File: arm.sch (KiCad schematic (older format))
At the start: 96 parts, among them J1 MICROSD_SOCKET_SPI, M1 MOTOR, P1 MicroUSB, P2 HC-05/06, Q1 MOSFET_N, Q2 IRLML2246TRPBF, Q3 IRLML2246TRPBF, Q5 IRLML2246TRPBF, Q6 IRLML2246TRPBF, Q7 IRLML2246TRPBF, Q8 IRLML2246TRPBF, Q9 IRLML2246TRPBF, U3 LTC2942-1, U4 HMC5883L, U5 MPU6050, U7 BMP085, X1 8 mHz, X2 32.768(MS3V-T1R)

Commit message: Rearranged MOSFET pullup resistors, ~CHARGE and ALERT moved to PC2 and PC3
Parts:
- added R? (x3): 300R, ~, symbol R
- R10, R12, R17, R20, R?: value 1M -> 100k
- R14, R18: value 10k -> 100k
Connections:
- net SD_CD is gone; now on net ~CHARGE: J1.9 (Card_Detect), U?.24 (ADC1_IN14/PC4)
- net ALERT: now also U?.10 (ADC1_IN12/PC2); no longer U?.2 (PC13/TAMPER_RTC)
- net NSS2: now also U?.51 (PC10); no longer U?.52 (PC11)
- net RING_O1: now also R?.2
- net RING_O2: now also R?.2
- net RING_O3: now also R?.2
- net ~CHARGE: now also U?.11 (ADC1_IN13/PC3); no longer U?.51 (PC10)
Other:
- moved on the sheet: D1, M1, Q2, R10, R7
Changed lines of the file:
@@
 P 4750 5200
 F 0 "R12" V 4830 5200 40  0000 C CNN
-F 1 "1M" V 4757 5201 40  0000 C CNN
+F 1 "100k" V 4757 5201 40  0000 C CNN
 F 2 "~" V 4680 5200 30  0000 C CNN
 F 3 "~" H 4750 5200 30  0000 C CNN
@@
 	1    0    0    -1
 $EndComp
-Text GLabel 7900 3600 2    60   Output ~ 0
+Text GLabel 8000 3600 2    60   Output ~ 0
 ~BT_PWR_ENABLE
-Text GLabel 4050 2400 0    60   Input ~ 0
+Text GLabel 7200 3550 2    60   Input ~ 0
 ALERT
 $Comp
@@
 L +3.3V #PWR033
 U 1 1 52E31088
-P 13850 2600
-F 0 "#PWR033" H 13850 2560 30  0001 C CNN
-F 1 "+3.3V" H 13850 2710 30  0000 C CNN
-F 2 "" H 13850 2600 60  0000 C CNN
-F 3 "" H 13850 2600 60  0000 C CNN
-	1    13850 2600
+P 4100 9000
+F 0 "#PWR033" H 4100 8960 30  0001 C CNN
+F 1 "+3.3V" H 4100 9110 30  0000 C CNN
+F 2 "" H 4100 9000 60  0000 C CNN
+F 3 "" H 4100 9000 60  0000 C CNN
+	1    4100 9000
 	1    0    0    -1
 $EndComp
@@
 L R R10
 U 1 1 52E3182F
-P 13500 3150
-F 0 "R10" V 13580 3150 40  0000 C CNN
-F 1 "1M" V 13507 3151 40  0000 C CNN
-F 2 "~" V 13430 3150 30  0000 C CNN
-F 3 "~" H 13500 3150 30  0000 C CNN
-	1    13500 3150
+P 3750 9550
+F 0 "R10" V 3830 9550 40  0000 C CNN
+F 1 "100k" V 3757 9551 40  0000 C CNN
+F 2 "~" V 3680 9550 30  0000 C CNN
+F 3 "~" H 3750 9550 30  0000 C CNN
+	1    3750 9550
 	0    -1   -1   0
 $EndComp
@@
 L R R7
 U 1 1 52E31D26
-P 12700 2250
-F 0 "R7" V 12780 2250 40  0000 C CNN
-F 1 "300R" V 12707 2251 40  0000 C CNN
-F 2 "~" V 12630 2250 30  0000 C CNN
-F 3 "~" H 12700 2250 30  0000 C CNN
-	1    12700 2250
-	1    0    0    -1
-$EndComp
-Text GLabel 13000 1850 2    60   Input ~ 0
+P 2250 9750
+F 0 "R7" V 2330 9750 40  0000 C CNN
+F 1 "300R" V 2257 9751 40  0000 C CNN
+F 2 "~" V 2180 9750 30  0000 C CNN
+F 3 "~" H 2250 9750 30  0000 C CNN
+	1    2250 9750
+	0    -1   -1   0
+$EndComp
+Text GLabel 1500 9750 0    60   Input ~ 0
 ~VIBRATION
 $Comp
@@
 L MOSFET_P Q2
 U 1 1 52EC203B
-P 13100 2750
-F 0 "Q2" H 13100 2940 60  0000 R CNN
-F 1 "IRLML2246TRPBF" H 13100 2570 60  0000 R CNN
-F 2 "~" H 13100 2750 60  0000 C CNN
-F 3 "http://www.irf.com/product-info/datasheets/data/irlml2246pbf.pdf" H 13100 2750 60  0001 C CNN
-	1    13100 2750
+P 3350 9150
+F 0 "Q2" H 3350 9340 60  0000 R CNN
+F 1 "IRLML2246TRPBF" H 3350 8970 60  0000 R CNN
+F 2 "~" H 3350 9150 60  0000 C CNN
+F 3 "http://www.irf.com/product-info/datasheets/data/irlml2246pbf.pdf" H 3350 9150 60  0001 C CNN
+	1    3350 9150
 	0    -1   -1   0
 $EndComp
@@
 L GND #PWR034
 U 1 1 52EC22C7
-P 11400 3150
-F 0 "#PWR034" H 11400 3150 30  0001 C CNN
-F 1 "GND" H 11400 3080 30  0001 C CNN
-F 2 "" H 11400 3150 60  0000 C CNN
-F 3 "" H 11400 3150 60  0000 C CNN
-	1    11400 3150
+P 1650 9550
+F 0 "#PWR034" H 1650 9550 30  0001 C CNN
+F 1 "GND" H 1650 9480 30  0001 C CNN
+F 2 "" H 1650 9550 60  0000 C CNN
+F 3 "" H 1650 9550 60  0000 C CNN
+	1    1650 9550
 	1    0    0    -1
 $EndComp
@@
 P 6900 5350
 F 0 "R14" V 6980 5350 40  0000 C CNN
-F 1 "10k" V 6907 5351 40  0000 C CNN
+F 1 "100k" V 6907 5351 40  0000 C CNN
 F 2 "~" V 6830 5350 30  0000 C CNN
 F 3 "~" H 6900 5350 30  0000 C CNN
@@
 	1    0    0    -1
 $EndComp
-Text GLabel 7900 3450 2    60   Output ~ 0
+Text GLabel 8000 3450 2    60   Output ~ 0
 ~SYS_PWR_ENABLE
 $Comp
@@
 L DIODE D1
 U 1 1 52E30BBB
-P 11950 3050
-F 0 "D1" H 11950 3150 40  0000 C CNN
-F 1 "DIODE" H 11950 2950 40  0000 C CNN
-F 2 "~" H 11950 3050 60  0000 C CNN
-F 3 "~" H 11950 3050 60  0000 C CNN
-	1    11950 3050
+P 2200 9450
+F 0 "D1" H 2200 9550 40  0000 C CNN
+F 1 "DIODE" H 2200 9350 40  0000 C CNN
+F 2 "~" H 2200 9450 60  0000 C CNN
+F 3 "~" H 2200 9450 60  0000 C CNN
+	1    2200 9450
 	1    0    0    -1
 $EndComp
@@
 P 7250 6350
 F 0 "R18" V 7330 6350 40  0000 C CNN
-F 1 "10k" V 7257 6351 40  0000 C CNN
+F 1 "100k" V 7257 6351 40  0000 C CNN
 F 2 "~" V 7180 6350 30  0000 C CNN
 F 3 "~" H 7250 6350 30  0000 C CNN
@@
 P 4750 5950
 F 0 "R17" V 4830 5950 40  0000 C CNN
-F 1 "1M" V 4757 5951 40  0000 C CNN
+F 1 "100k" V 4757 5951 40  0000 C CNN
 F 2 "~" V 4680 5950 30  0000 C CNN
 F 3 "~" H 4750 5950 30  0000 C CNN
@@
 P 4750 6700
 F 0 "R20" V 4830 6700 40  0000 C CNN
-F 1 "1M" V 4757 6701 40  0000 C CNN
+F 1 "100k" V 4757 6701 40  0000 C CNN
 F 2 "~" V 4680 6700 30  0000 C CNN
 F 3 "~" H 4750 6700 30  0000 C CNN
@@
 Text Label 4300 6950 0    60   ~ 0
 RING_O3
-Entry Wire Line
-	3900 5350 4000 5450
-Entry Wire Line
-	3900 6100 4000 6200
-Entry Wire Line
-	3900 6850 4000 6950
 $Comp
 L MOTOR M1
 U 1 1 5308D64D
-P 11950 2650
-F 0 "M1" H 11950 2750 60  0000 C CNN
-F 1 "MOTOR" H 11950 2550 60  0000 C CNN
-F 2 "" H 11950 2650 60  0000 C CNN
-F 3 "" H 11950 2650 60  0000 C CNN
-	1    11950 2650
+P 2200 9050
+F 0 "M1" H 2200 9150 60  0000 C CNN
+F 1 "MOTOR" H 2200 8950 60  0000 C CNN
+F 2 "" H 2200 9050 60  0000 C CNN
+F 3 "" H 2200 9050 60  0000 C CNN
+	1    2200 9050
 	-1   0    0    1
 $EndComp
@@
 P 3250 10600
 F 0 "R?" V 3330 10600 40  0000 C CNN
-F 1 "1M" V 3257 10601 40  0000 C CNN
+F 1 "100k" V 3257 10601 40  0000 C CNN
 F 2 "~" V 3180 10600 30  0000 C CNN
 F 3 "~" H 3250 10600 30  0000 C CNN
@@
 Text GLabel 7300 4500 3    60   Output ~ 0
 NSS2
-Text GLabel 7900 3300 2    60   Output ~ 0
+Text GLabel 8000 3300 2    60   Output ~ 0
 ~PWM_MODE
 $Comp
@@
 	6150 6750 6150 6600
 Wire Bus Line
-	3900 5350 3900 7700
-Wire Bus Line
-	3900 7700 5750 7700
+	3400 7700 5750 7700
 Wire Bus Line
 	5750 7700 5750 6950
@@
 	12600 7750 12600 7950
 Wire Wire Line
-	12500 2650 12500 3050
-Wire Wire Line
-	12900 2650 12500 2650
+	2750 9050 2750 9450
+Wire Wire Line
+	3150 9050 2750 9050
 Wire Wire Line
 	5450 6650 5350 6650
@@
 	700  1200 700  1350
 Wire Wire Line
-	4050 2400 4100 2400
+	7200 3550 7150 3550
 Wire Wire Line
 	11300 9100 11300 9900
@@
 	15350 5400 15350 4800
 Wire Wire Line
-	11400 2650 11400 3150
-Wire Wire Line
-	13300 2650 13850 2650
-Wire Wire Line
-	13850 3150 13750 3150
-Wire Wire Line
-	12700 3150 13250 3150
-Wire Wire Line
-	13100 3150 13100 2950
-Wire Wire Line
-	12700 2500 12700 3150
-Connection ~ 13100 3150
-Wire Wire Line
-	12700 2000 12700 1850
-Wire Wire Line
-	12700 1850 13000 1850
-Wire Wire Line
-	13850 2600 13850 3150
-Connection ~ 13850 2650
+	1650 9050 1650 9550
+Wire Wire Line
+	3550 9050 4100 9050
+Wire Wire Line
+	4100 9550 4000 9550
+Wire Wire Line
+	2950 9550 3500 9550
+Wire Wire Line
+	3350 9550 3350 9350
+Connection ~ 3350 9550
+Wire Wire Line
+	4100 9000 4100 9550
+Connection ~ 4100 9050
 Wire Wire Line
 	14200 5800 14200 6600
@@
 Wire Wire Line
 	1300 6250 1300 6300
-Connection ~ 11400 3050
-Wire Wire Line
-	11400 3050 11750 3050
-Wire Wire Line
-	12500 3050 12150 3050
+Connection ~ 1650 9450
+Wire Wire Line
+	1650 9450 2000 9450
+Wire Wire Line
+	2750 9450 2400 9450
 Wire Wire Line
 	1300 5750 1300 5550
@@
 	8000 4100 7100 4100
 Wire Wire Line
-	7900 3300 7750 3300
-Wire Wire Line
-	7750 3300 7750 3800
-Wire Wire Line
-	7750 3800 7100 3800
+	8000 3300 7850 3300
+Wire Wire Line
+	7850 3300 7850 3800
+Wire Wire Line
+	7850 3800 7100 3800
 Wire Wire Line
 	7300 3150 7100 3150
@@
 I2C_EXTRA2
 Wire Wire Line
-	7900 3450 7800 3450
-Wire Wire Line
-	7800 3450 7800 3900
-Wire Wire Line
-	7800 3900 7100 3900
-Wire Wire Line
-	7900 3600 7850 3600
-Wire Wire Line
-	7850 3600 7850 4000
-Wire Wire Line
-	7850 4000 7100 4000
-Wire Wire Line
-	7300 4500 7300 4400
+	8000 3450 7900 3450
+Wire Wire Line
+	7900 3450 7900 3900
+Wire Wire Line
+	7900 3900 7100 3900
+Wire Wire Line
+	8000 3600 7950 3600
+Wire Wire Line
+	7950 3600 7950 4000
+Wire Wire Line
+	7950 4000 7100 4000
+Wire Wire Line
+	7300 4300 7300 4500
 Wire Wire Line
 	8050 4200 8050 3900
@@
 	8050 3900 8200 3900
 Wire Wire Line
-	7300 4400 7100 4400
-Wire Wire Line
-	7100 4300 7450 4300
-Wire Wire Line
-	7450 4300 7450 4500
+	7450 3750 7450 4500
 Connection ~ 11700 8550
 Wire Wire Line
@@
 Wire Wire Line
 	8600 2800 8600 3150
+$Comp
+L R R?
+U 1 1 53A21C97
+P 3750 5450
+F 0 "R?" V 3830 5450 40  0000 C CNN
+F 1 "300R" V 3757 5451 40  0000 C CNN
+F 2 "~" V 3680 5450 30  0000 C CNN
+F 3 "~" H 3750 5450 30  0000 C CNN
+	1    3750 5450
+	0    -1   -1   0
+$EndComp
+$Comp
+L R R?
+U 1 1 53A21C9D
+P 3750 6200
+F 0 "R?" V 3830 6200 40  0000 C CNN
+F 1 "300R" V 3757 6201 40  0000 C CNN
+F 2 "~" V 3680 6200 30  0000 C CNN
+F 3 "~" H 3750 6200 30  0000 C CNN
+	1    3750 6200
+	0    -1   -1   0
+$EndComp
+$Comp
+L R R?
+U 1 1 53A21CA3
+P 3750 6950
+F 0 "R?" V 3830 6950 40  0000 C CNN
+F 1 "300R" V 3757 6951 40  0000 C CNN
+F 2 "~" V 3680 6950 30  0000 C CNN
+F 3 "~" H 3750 6950 30  0000 C CNN
+	1    3750 6950
+	0    -1   -1   0
+$EndComp
+Entry Wire Line
+	3400 5550 3500 5450
+Entry Wire Line
+	3400 6300 3500 6200
+Entry Wire Line
+	3400 7050 3500 6950
+Wire Bus Line
+	3400 5550 3400 7700
+Wire Wire Line
+	2500 9750 2950 9750
+Wire Wire Line
+	2950 9750 2950 9550
+Wire Wire Line
+	1500 9750 2000 9750
+Wire Wire Line
+	7100 3500 7150 3500
+Wire Wire Line
+	7150 3500 7150 3550
+Wire Wire Line
+	7450 3750 7150 3750
+Wire Wire Line
+	7150 3750 7150 3600
+Wire Wire Line
+	7150 3600 7100 3600
+Wire Wire Line
+	7100 4300 7300 4300
 $EndSCHEMATC

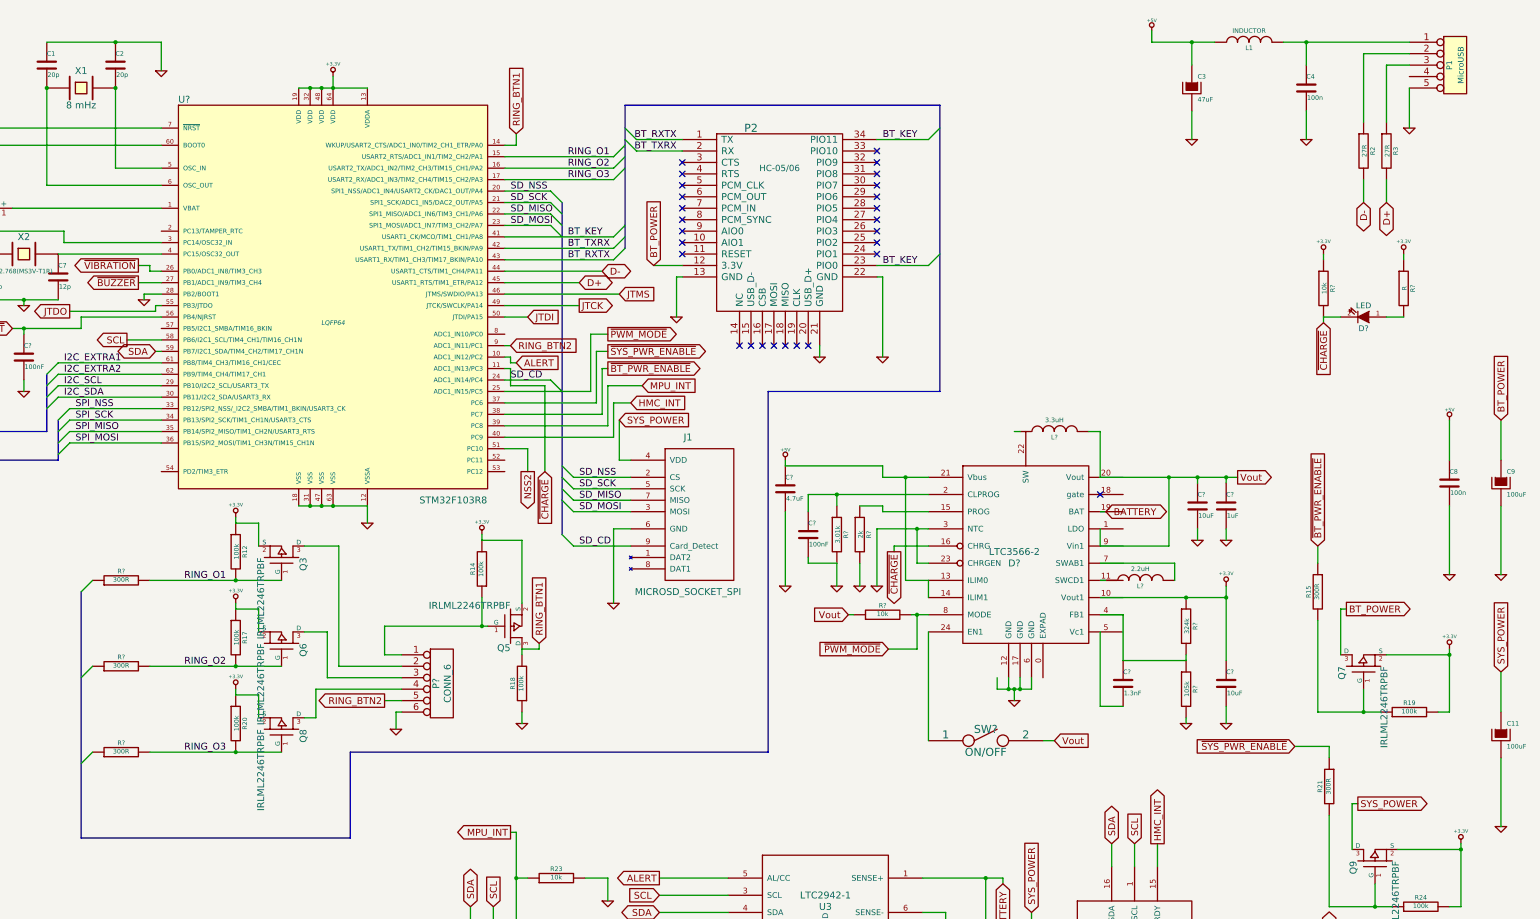
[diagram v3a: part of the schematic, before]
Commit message: schematic layout changes because Plex-Daniel wanted so...
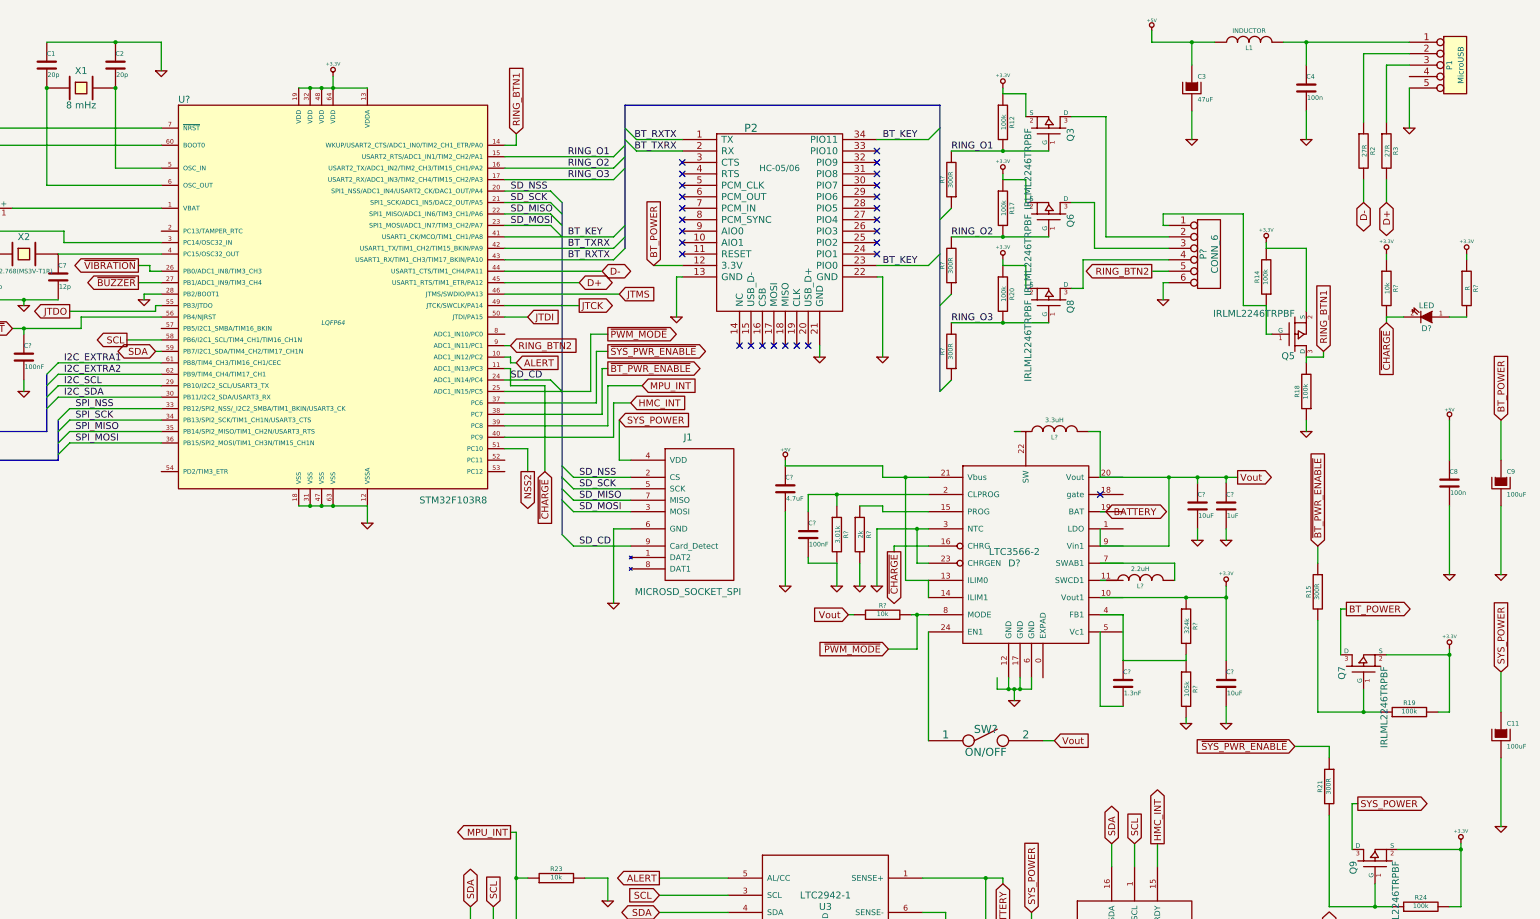
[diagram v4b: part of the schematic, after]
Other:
- moved on the sheet: D?, P?, Q3, Q5, Q6, Q8, R12, R14, R17, R18, R20, R?

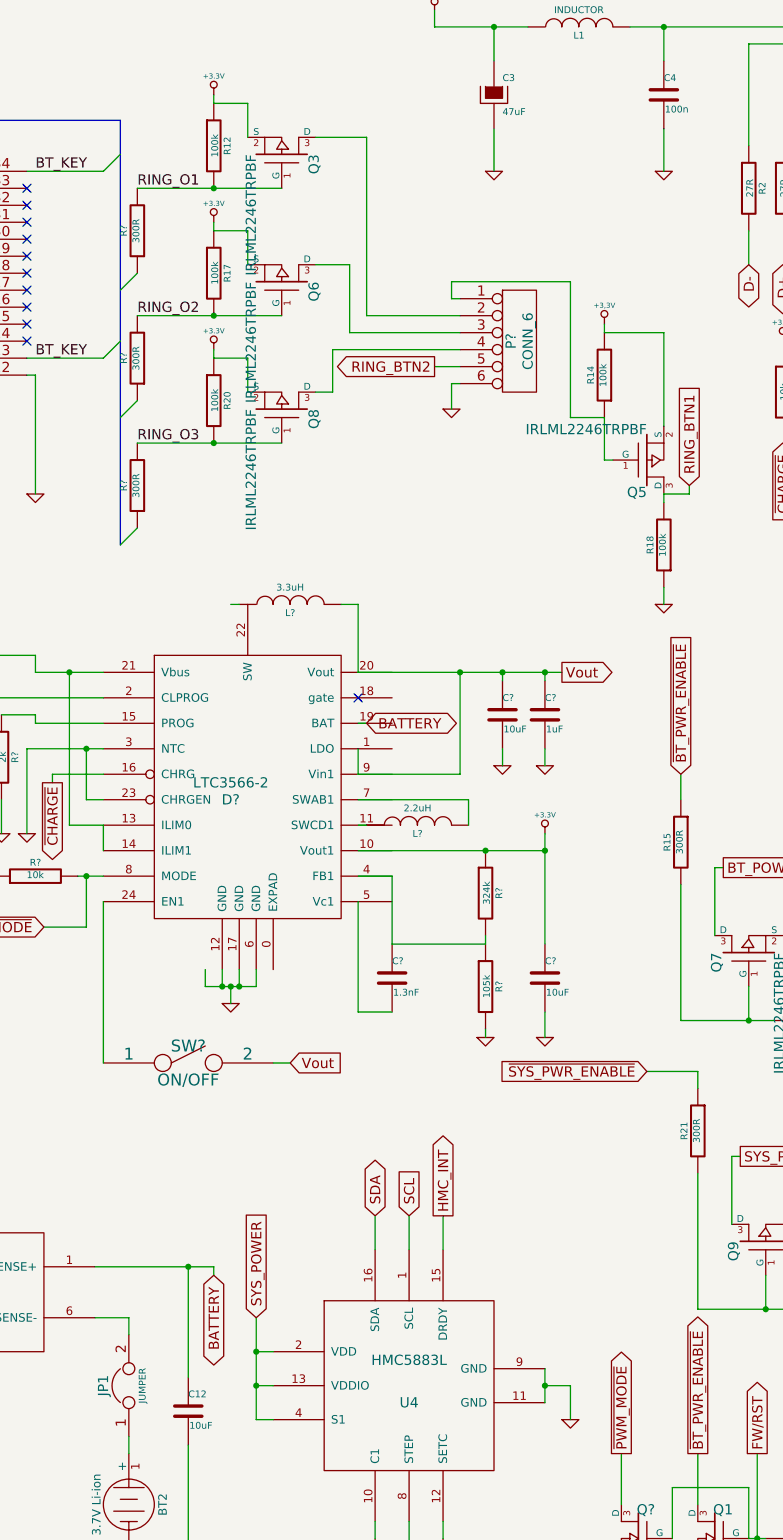
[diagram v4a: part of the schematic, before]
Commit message: Fixed LTC3566 (EXPAD pin number set to 0, made component wider, so that all text would fit)
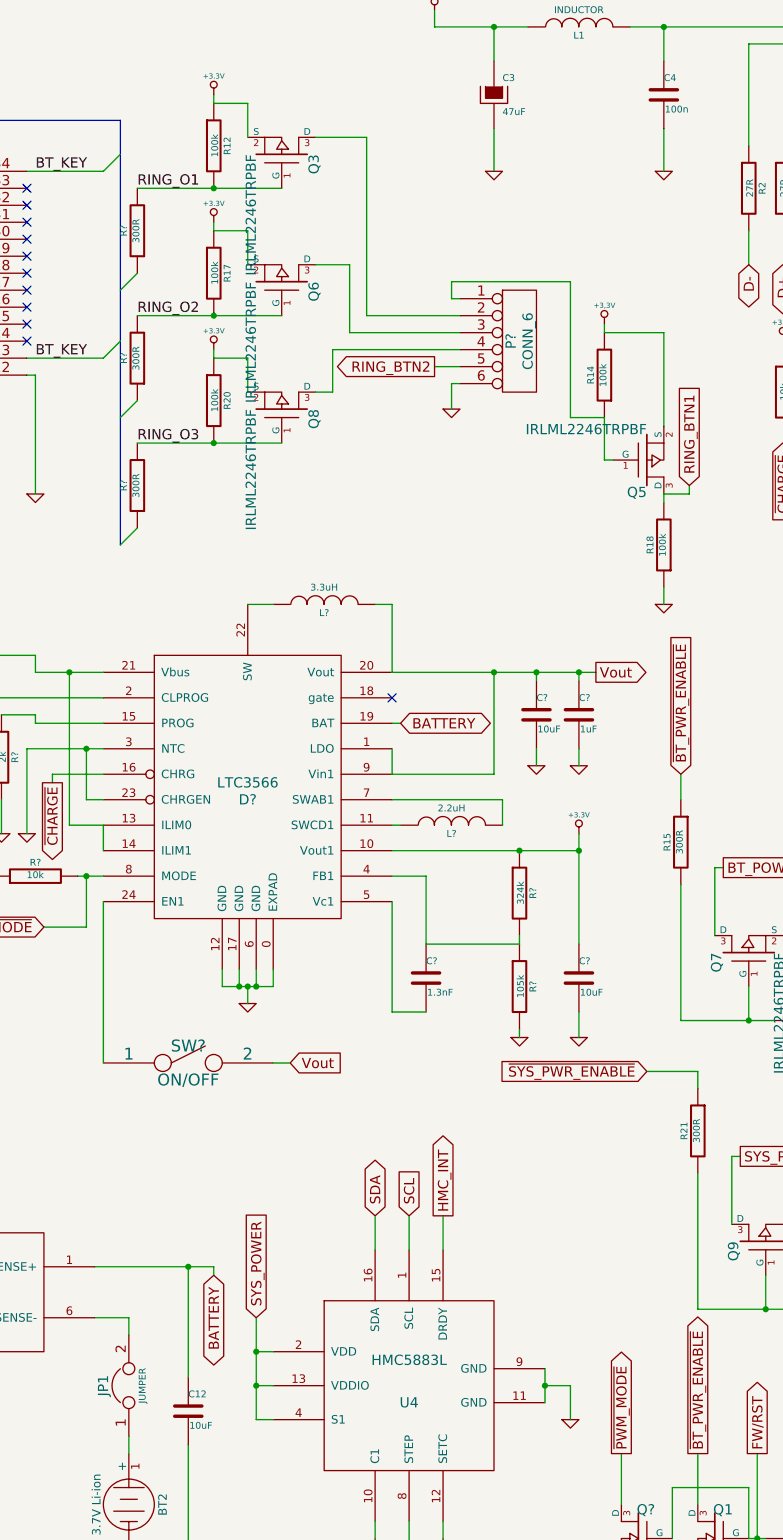
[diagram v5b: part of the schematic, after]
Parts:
- removed D?: LTC3566-2, symbol LTC3566
- added D?: LTC3566, ~, symbol LTC3566
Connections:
- net +3.3V: now also D?.10 (Vout1)
- net +5V: now also D?.13 (ILIM0), D?.14 (ILIM1), D?.21 (Vbus)
- net BATTERY: now also D?.19 (BAT)
- net GND: now also D?.0 (EXPAD), D?.12 (GND), D?.17 (GND), D?.23 (CHRGEN), D?.3 (NTC), D?.6 (GND)
- net Vout: now also D?.1 (LDO), D?.20 (Vout), D?.9 (Vin1)
- net ~CHARGE: now also D?.16 (CHRG)
- net ~PWM_MODE: now also D?.8 (MODE)
- net at R?.1: now also D?.15 (PROG)
- net at C?.1, R?.1: now also D?.2 (CLPROG)
- net at SW?.1: now also D?.24 (EN1)
- net at C?.1, R?.1, R?.2: now also D?.4 (FB1)
- net at L?.1: now also D?.22 (SW)
- net at C?.2: now also D?.5 (Vc1)
- net at L?.1: now also D?.11 (SWCD1)
- net at L?.2: now also D?.7 (SWAB1)
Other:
- moved on the sheet: C?, L?, R?
